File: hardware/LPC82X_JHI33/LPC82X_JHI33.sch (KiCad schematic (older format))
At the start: 24 parts, among them J1 Conn_02x09_Odd_Even, J2 Conn_02x09_Odd_Even, J3 JTAG_2X05, U1 LPC824M201JHI33, Y1 12MHz

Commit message: LPC824 QFN33 new footprint for LPC and shrunk paste size
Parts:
- N2: value 20181124 -> 20190313
- U1: footprint SquantorIC:SOT617-3 -> SquantorIC:SOT617-3_alt_paste
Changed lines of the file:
@@
 EESchema Schematic File Version 4
-LIBS:LPC82X_JHI33_2layer-cache
+LIBS:LPC82X_JHI33-cache
 EELAYER 26 0
 EELAYER END
@@
 P 4000 1650
 F 0 "N2" H 4000 1750 60  0000 C CNN
-F 1 "20181124" H 4000 1650 60  0000 C CNN
+F 1 "20190313" H 4000 1650 60  0000 C CNN
 F 2 "SquantorLabels:Label_version" H 4000 1650 60  0001 C CNN
 F 3 "" H 4000 1650 60  0001 C CNN
@@
 F 0 "U1" H 7077 5242 45  0000 L CNN
 F 1 "LPC824M201JHI33" H 7077 5158 45  0000 L CNN
-F 2 "SquantorIC:SOT617-3" H 7450 4300 20  0001 C CNN
+F 2 "SquantorIC:SOT617-3_alt_paste" H 7450 4300 20  0001 C CNN
 F 3 "" H 6250 5100 60  0000 C CNN
 	1    6900 5200
@@
 F 0 "U1" H 7169 1942 45  0000 L CNN
 F 1 "LPC824M201JHI33" H 7169 1858 45  0000 L CNN
-F 2 "SquantorIC:SOT617-3" H 7000 1000 20  0001 C CNN
+F 2 "SquantorIC:SOT617-3_alt_paste" H 7000 1000 20  0001 C CNN
 F 3 "" H 5800 1800 60  0000 C CNN
 	2    6450 1900
@@
 F 0 "U1" H 7119 3592 45  0000 L CNN
 F 1 "LPC824M201JHI33" H 7119 3508 45  0000 L CNN
-F 2 "SquantorIC:SOT617-3" H 7050 2650 20  0001 C CNN
+F 2 "SquantorIC:SOT617-3_alt_paste" H 7050 2650 20  0001 C CNN
 F 3 "" H 5850 3450 60  0000 C CNN
 	3    6500 3550

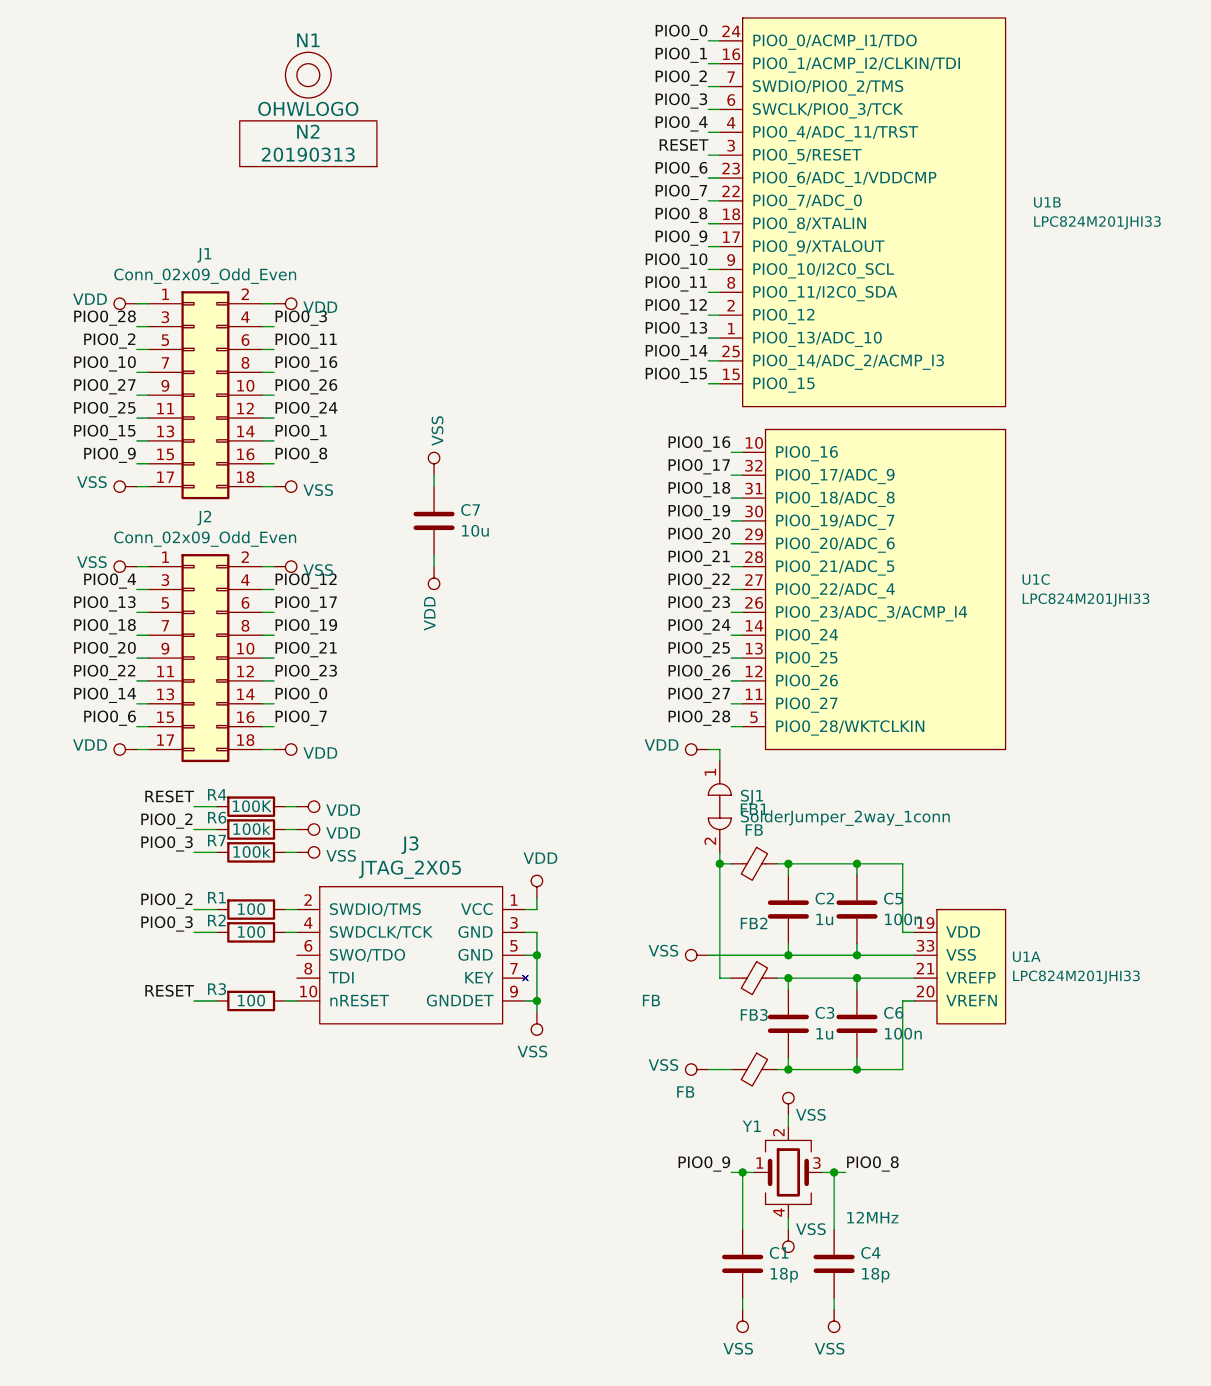
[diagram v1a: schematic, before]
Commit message: changed net names, added named connectors
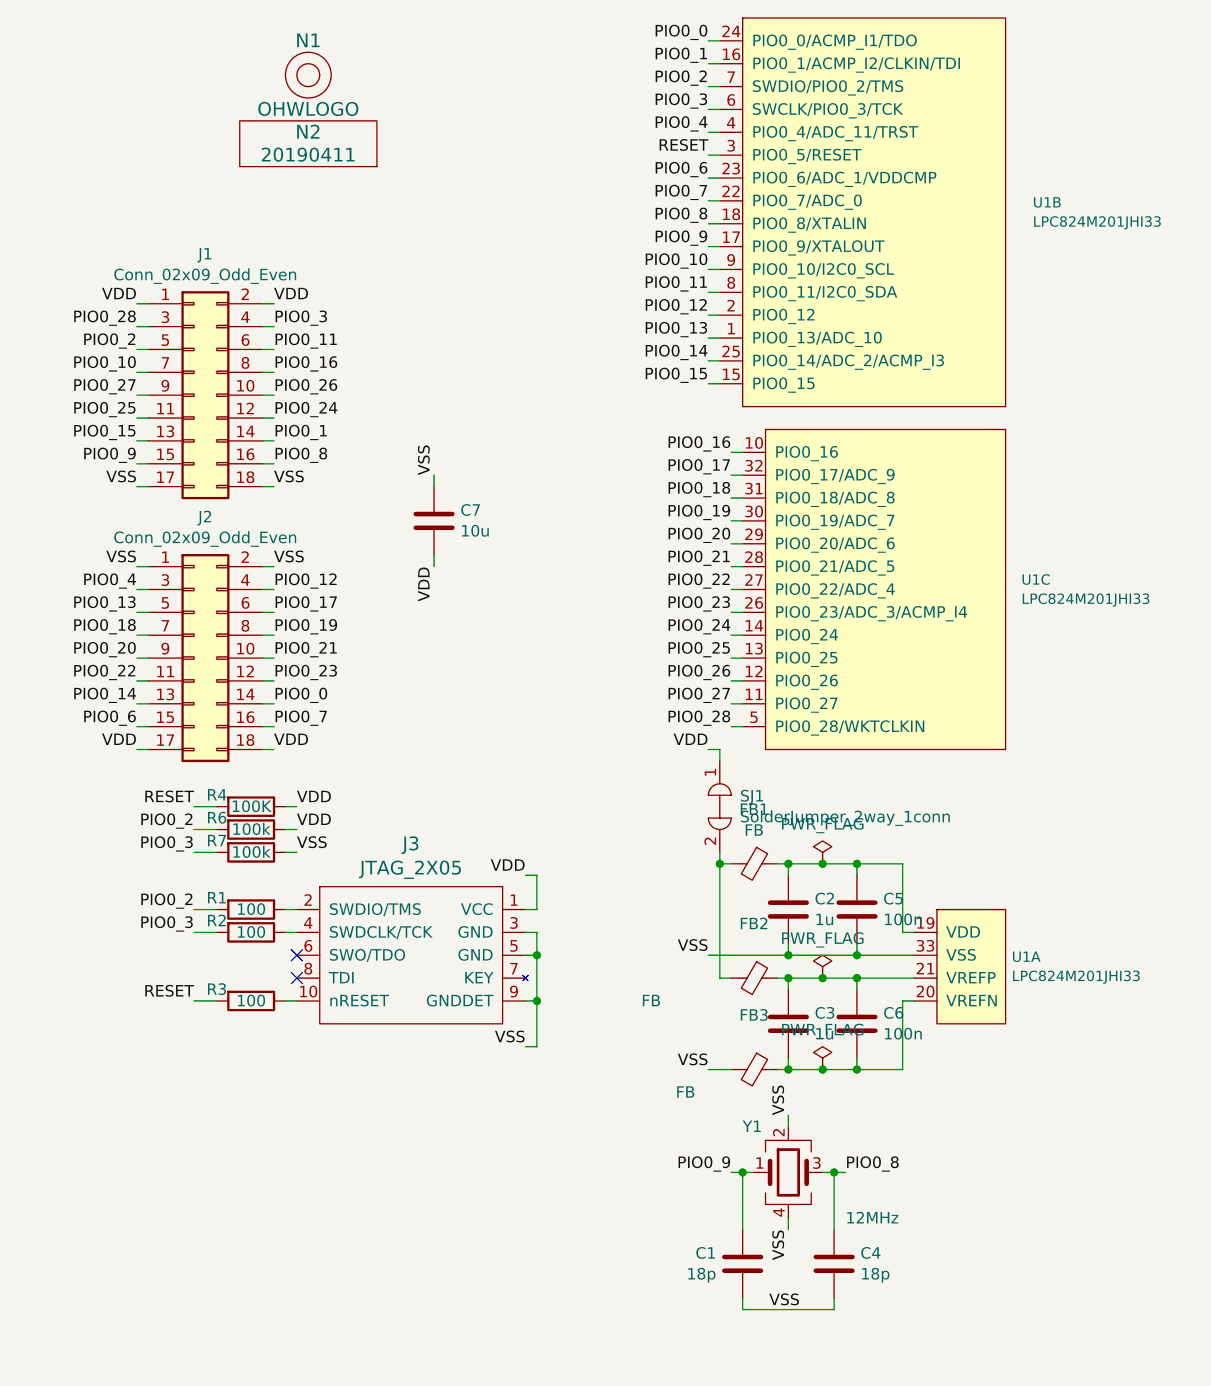
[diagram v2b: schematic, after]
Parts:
- N2: value 20190313 -> 20190411
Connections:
- no-connect marks 0 -> 2

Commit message: changed connectors, newer component library
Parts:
- J1: value Conn_02x09_Odd_Even -> LPC82XJHI33_LEFT; footprint SquantorConnectors:Header-0254-2X09-H010 -> SquantorConnectorsNamed:LPC82XJHI33_breakout_left; symbol Connector_Generic:Conn_02x09_Odd_Even -> SquantorConnectorsNamed:LPC82XJHI33_breakout_left
- J2: value Conn_02x09_Odd_Even -> LPC82XJHI33_RIGHT; footprint SquantorConnectors:Header-0254-2X09-H010 -> SquantorConnectorsNamed:LPC82XJHI33_breakout_right; symbol Connector_Generic:Conn_02x09_Odd_Even -> SquantorConnectorsNamed:LPC82XJHI33_breakout_right
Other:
- moved on the sheet: J1, J2
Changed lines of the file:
@@
 	5850 5650 5750 5650
 $Comp
-L Connector_Generic:Conn_02x09_Odd_Even J1
+L SquantorConnectorsNamed:LPC82XJHI33_breakout_left J1
 U 1 1 5BD2E6A6
-P 3500 2700
-F 0 "J1" H 3550 3317 50  0000 C CNN
-F 1 "Conn_02x09_Odd_Even" H 3550 3226 50  0000 C CNN
-F 2 "SquantorConnectors:Header-0254-2X09-H010" H 3500 2700 50  0001 C CNN
-F 3 "~" H 3500 2700 50  0001 C CNN
-	1    3500 2700
-	1    0    0    -1
-$EndComp
-$Comp
-L Connector_Generic:Conn_02x09_Odd_Even J2
+P 3600 2600
+F 0 "J1" H 3600 3265 50  0000 C CNN
+F 1 "LPC82XJHI33_LEFT" H 3600 3174 50  0000 C CNN
+F 2 "SquantorConnectorsNamed:LPC82XJHI33_breakout_left" H 3600 2600 50  0001 C CNN
+F 3 "~" H 3600 2600 50  0001 C CNN
+	1    3600 2600
+	1    0    0    -1
+$EndComp
+$Comp
+L SquantorConnectorsNamed:LPC82XJHI33_breakout_right J2
 U 1 1 5BD2E711
-P 3500 3850
-F 0 "J2" H 3550 4467 50  0000 C CNN
-F 1 "Conn_02x09_Odd_Even" H 3550 4376 50  0000 C CNN
-F 2 "SquantorConnectors:Header-0254-2X09-H010" H 3500 3850 50  0001 C CNN
-F 3 "~" H 3500 3850 50  0001 C CNN
-	1    3500 3850
-	1    0    0    -1
-$EndComp
-Wire Wire Line
-	3250 2300 3300 2300
-Wire Wire Line
-	3850 2300 3800 2300
-Wire Wire Line
-	3250 3450 3300 3450
-Wire Wire Line
-	3800 3450 3850 3450
+P 3600 3850
+F 0 "J2" H 3600 4515 50  0000 C CNN
+F 1 "LPC82XJHI33_RIGHT" H 3600 4424 50  0000 C CNN
+F 2 "SquantorConnectorsNamed:LPC82XJHI33_breakout_right" H 3600 3850 50  0001 C CNN
+F 3 "~" H 3600 3850 50  0001 C CNN
+	1    3600 3850
+	1    0    0    -1
+$EndComp
+Wire Wire Line
+	3100 2200 3150 2200
+Wire Wire Line
+	4100 2200 4050 2200
+Wire Wire Line
+	3100 3450 3150 3450
+Wire Wire Line
+	4050 3450 4100 3450
 $Comp
 L SquantorConnectors:JTAG_2X05 J3
@@
 PIO0_28
 Wire Wire Line
-	3300 2400 3250 2400
-Wire Wire Line
-	3850 2400 3800 2400
-Wire Wire Line
-	3300 2500 3250 2500
-Wire Wire Line
-	3300 2600 3250 2600
-Wire Wire Line
-	3300 2700 3250 2700
-Wire Wire Line
-	3300 2800 3250 2800
-Wire Wire Line
-	3300 2900 3250 2900
-Wire Wire Line
-	3300 3000 3250 3000
-Wire Wire Line
-	3300 3100 3250 3100
-Wire Wire Line
-	3800 2500 3850 2500
-Wire Wire Line
-	3800 2600 3850 2600
-Wire Wire Line
-	3800 2700 3850 2700
-Wire Wire Line
-	3800 2800 3850 2800
-Wire Wire Line
-	3800 2900 3850 2900
-Wire Wire Line
-	3800 3000 3850 3000
-Wire Wire Line
-	3800 3100 3850 3100
-Text Label 3250 2400 2    50   ~ 0
+	3150 2300 3100 2300
+Wire Wire Line
+	4100 2300 4050 2300
+Wire Wire Line
+	3150 2400 3100 2400
+Wire Wire Line
+	3150 2500 3100 2500
+Wire Wire Line
+	3150 2600 3100 2600
+Wire Wire Line
+	3150 2700 3100 2700
+Wire Wire Line
+	3150 2800 3100 2800
+Wire Wire Line
+	3150 2900 3100 2900
+Wire Wire Line
+	3150 3000 3100 3000
+Wire Wire Line
+	4050 2400 4100 2400
+Wire Wire Line
+	4050 2500 4100 2500
+Wire Wire Line
+	4050 2600 4100 2600
+Wire Wire Line
+	4050 2700 4100 2700
+Wire Wire Line
+	4050 2800 4100 2800
+Wire Wire Line
+	4050 2900 4100 2900
+Wire Wire Line
+	4050 3000 4100 3000
+Text Label 3100 2300 2    50   ~ 0
 PIO0_28
-Text Label 3850 2400 0    50   ~ 0
+Text Label 4100 2300 0    50   ~ 0
 PIO0_3
-Text Label 3250 2500 2    50   ~ 0
+Text Label 3100 2400 2    50   ~ 0
 PIO0_2
-Text Label 3850 2500 0    50   ~ 0
+Text Label 4100 2400 0    50   ~ 0
 PIO0_11
-Text Label 3250 2600 2    50   ~ 0
+Text Label 3100 2500 2    50   ~ 0
 PIO0_10
-Text Label 3850 2600 0    50   ~ 0
+Text Label 4100 2500 0    50   ~ 0
 PIO0_16
-Text Label 3250 2700 2    50   ~ 0
+Text Label 3100 2600 2    50   ~ 0
 PIO0_27
-Text Label 3850 2700 0    50   ~ 0
+Text Label 4100 2600 0    50   ~ 0
 PIO0_26
-Text Label 3250 2800 2    50   ~ 0
+Text Label 3100 2700 2    50   ~ 0
 PIO0_25
-Text Label 3850 2800 0    50   ~ 0
+Text Label 4100 2700 0    50   ~ 0
 PIO0_24
-Text Label 3250 2900 2    50   ~ 0
+Text Label 3100 2800 2    50   ~ 0
 PIO0_15
-Text Label 3850 2900 0    50   ~ 0
+Text Label 4100 2800 0    50   ~ 0
 PIO0_1
-Text Label 3250 3000 2    50   ~ 0
+Text Label 3100 2900 2    50   ~ 0
 PIO0_9
-Text Label 3850 3000 0    50   ~ 0
+Text Label 4100 2900 0    50   ~ 0
 PIO0_8
 Wire Wire Line
-	3250 3550 3300 3550
-Wire Wire Line
-	3300 3650 3250 3650
-Wire Wire Line
-	3250 3750 3300 3750
-Wire Wire Line
-	3300 3850 3250 3850
-Wire Wire Line
-	3300 3950 3250 3950
-Wire Wire Line
-	3300 4050 3250 4050
-Wire Wire Line
-	3300 4150 3250 4150
-Wire Wire Line
-	3300 4250 3250 4250
-Wire Wire Line
-	3800 4250 3850 4250
-Wire Wire Line
-	3850 4150 3800 4150
-Wire Wire Line
-	3800 4050 3850 4050
-Wire Wire Line
-	3850 3950 3800 3950
-Wire Wire Line
-	3800 3850 3850 3850
-Wire Wire Line
-	3850 3750 3800 3750
-Wire Wire Line
-	3800 3650 3850 3650
-Wire Wire Line
-	3850 3550 3800 3550
-Text Label 3850 4150 0    50   ~ 0
+	3100 3550 3150 3550
+Wire Wire Line
+	3150 3650 3100 3650
+Wire Wire Line
+	3100 3750 3150 3750
+Wire Wire Line
+	3150 3850 3100 3850
+Wire Wire Line
+	3150 3950 3100 3950
+Wire Wire Line
+	3150 4050 3100 4050
+Wire Wire Line
+	3150 4150 3100 4150
+Wire Wire Line
+	3150 4250 3100 4250
+Wire Wire Line
+	4050 4250 4100 4250
+Wire Wire Line
+	4100 4150 4050 4150
+Wire Wire Line
+	4050 4050 4100 4050
+Wire Wire Line
+	4100 3950 4050 3950
+Wire Wire Line
+	4050 3850 4100 3850
+Wire Wire Line
+	4100 3750 4050 3750
+Wire Wire Line
+	4050 3650 4100 3650
+Wire Wire Line
+	4100 3550 4050 3550
+Text Label 4100 4150 0    50   ~ 0
 PIO0_7
-Text Label 3250 4150 2    50   ~ 0
+Text Label 3100 4150 2    50   ~ 0
 PIO0_6
-Text Label 3850 4050 0    50   ~ 0
+Text Label 4100 4050 0    50   ~ 0
 PIO0_0
-Text Label 3250 4050 2    50   ~ 0
+Text Label 3100 4050 2    50   ~ 0
 PIO0_14
-Text Label 3850 3950 0    50   ~ 0
+Text Label 4100 3950 0    50   ~ 0
 PIO0_23
-Text Label 3250 3950 2    50   ~ 0
+Text Label 3100 3950 2    50   ~ 0
 PIO0_22
-Text Label 3850 3850 0    50   ~ 0
+Text Label 4100 3850 0    50   ~ 0
 PIO0_21
-Text Label 3250 3850 2    50   ~ 0
+Text Label 3100 3850 2    50   ~ 0
 PIO0_20
-Text Label 3850 3750 0    50   ~ 0
+Text Label 4100 3750 0    50   ~ 0
 PIO0_19
-Text Label 3250 3750 2    50   ~ 0
+Text Label 3100 3750 2    50   ~ 0
 PIO0_18
-Text Label 3850 3650 0    50   ~ 0
+Text Label 4100 3650 0    50   ~ 0
 PIO0_17
-Text Label 3250 3650 2    50   ~ 0
+Text Label 3100 3650 2    50   ~ 0
 PIO0_13
-Text Label 3850 3550 0    50   ~ 0
+Text Label 4100 3550 0    50   ~ 0
 PIO0_12
-Text Label 3250 3550 2    50   ~ 0
+Text Label 3100 3550 2    50   ~ 0
 PIO0_4
 $Comp
@@
 Wire Wire Line
 	5800 4250 5750 4250
-Text Label 3250 2300 2    50   ~ 0
+Text Label 3100 2200 2    50   ~ 0
 VDD
-Text Label 3850 2300 0    50   ~ 0
+Text Label 4100 2200 0    50   ~ 0
 VDD
-Text Label 3250 3100 2    50   ~ 0
+Text Label 3100 3000 2    50   ~ 0
 VSS
-Text Label 3850 3100 0    50   ~ 0
+Text Label 4100 3000 0    50   ~ 0
 VSS
-Text Label 3250 3450 2    50   ~ 0
+Text Label 3100 3450 2    50   ~ 0
 VSS
-Text Label 3850 3450 0    50   ~ 0
+Text Label 4100 3450 0    50   ~ 0
 VSS
-Text Label 3250 4250 2    50   ~ 0
+Text Label 3100 4250 2    50   ~ 0
 VDD
-Text Label 3850 4250 0    50   ~ 0
+Text Label 4100 4250 0    50   ~ 0
 VDD
 Text Label 4550 3050 1    50   ~ 0

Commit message: silk placement completed
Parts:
- N2: value 20190411 -> 20190412
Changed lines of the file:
@@
 P 4000 1650
 F 0 "N2" H 4000 1750 60  0000 C CNN
-F 1 "20190411" H 4000 1650 60  0000 C CNN
+F 1 "20190412" H 4000 1650 60  0000 C CNN
 F 2 "SquantorLabels:Label_version" H 4000 1650 60  0001 C CNN
 F 3 "" H 4000 1650 60  0001 C CNN

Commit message: updated versionnumber
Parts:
- N2: value 20190412 -> 20190514
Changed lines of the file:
@@
 P 4000 1650
 F 0 "N2" H 4000 1750 60  0000 C CNN
-F 1 "20190412" H 4000 1650 60  0000 C CNN
+F 1 "20190514" H 4000 1650 60  0000 C CNN
 F 2 "SquantorLabels:Label_version" H 4000 1650 60  0001 C CNN
 F 3 "" H 4000 1650 60  0001 C CNN
